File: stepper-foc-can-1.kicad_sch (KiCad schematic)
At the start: 31 parts, among them J1 TC2030, J2 Conn_01x02, U1 STM32G474RBTx, U2 MX25947, Y1 Crystal_GND24

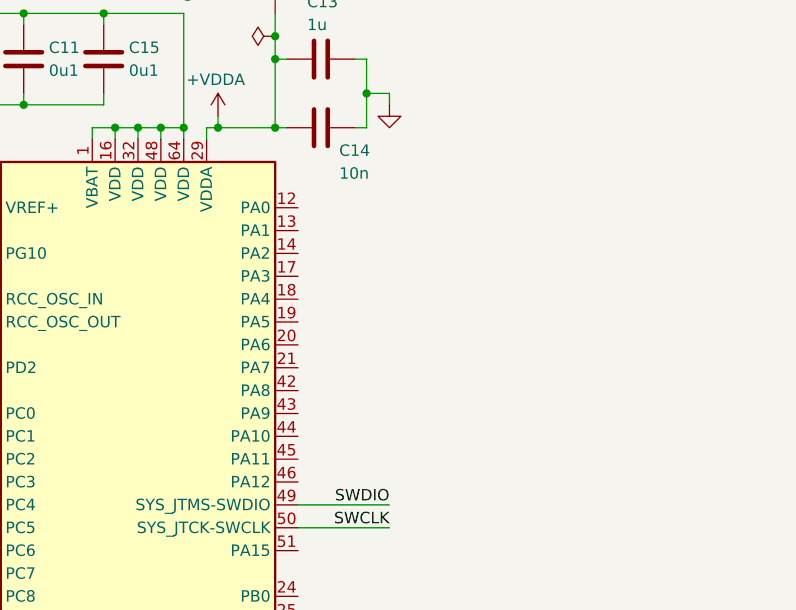
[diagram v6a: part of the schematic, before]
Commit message: schem: add uart connctor
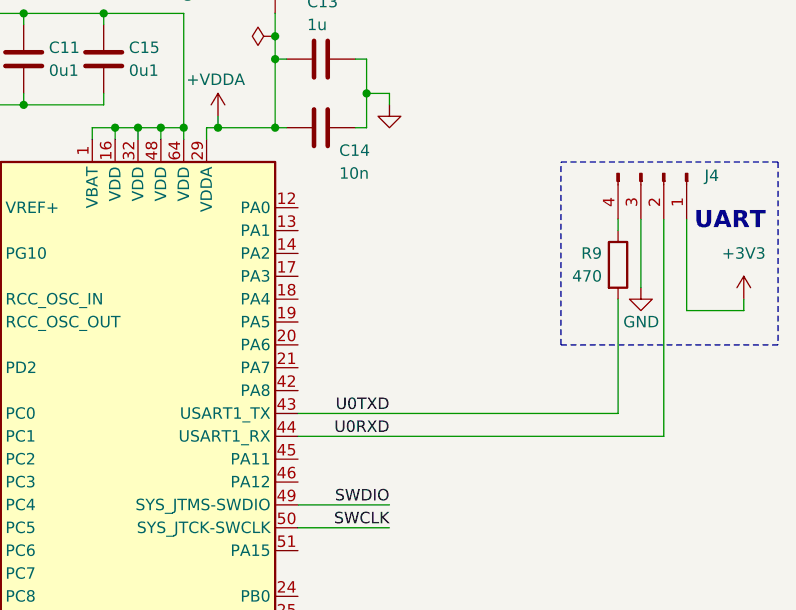
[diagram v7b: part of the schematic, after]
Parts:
- added J4: Conn_01x04_Pin, Connector_PinHeader_2.54mm:PinHeader_1x04_P2.54mm_Vertical, symbol Connector:Conn_01x04_Pin
- added R9: 470, Resistor_SMD:R_0402_1005Metric, symbol Device:R
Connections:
- net +3V3: now also J4.1 (Pin_1)
- net GND: now also J4.3 (Pin_3)
- net U0TXD: now reaches U1.43 (PA9)
- net U0TXD: now also R9.2
- net U0RXD: now reaches U1.44 (PA10)
- net U0RXD: now also J4.2 (Pin_2)
- new net: J4.4 (Pin_4), R9.1
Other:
- note added: "UART"

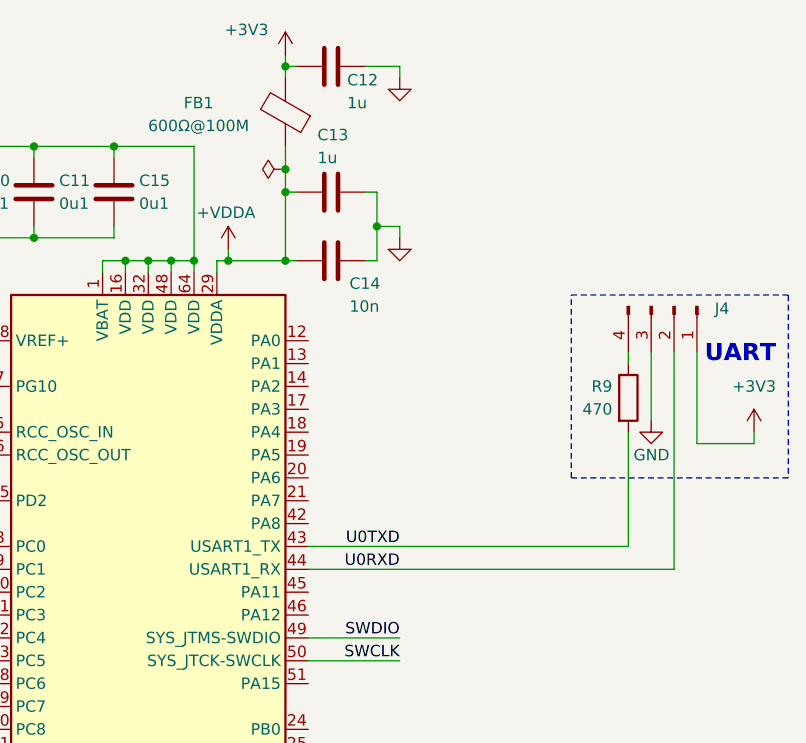
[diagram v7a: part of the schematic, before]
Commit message: schem: fix uart pins
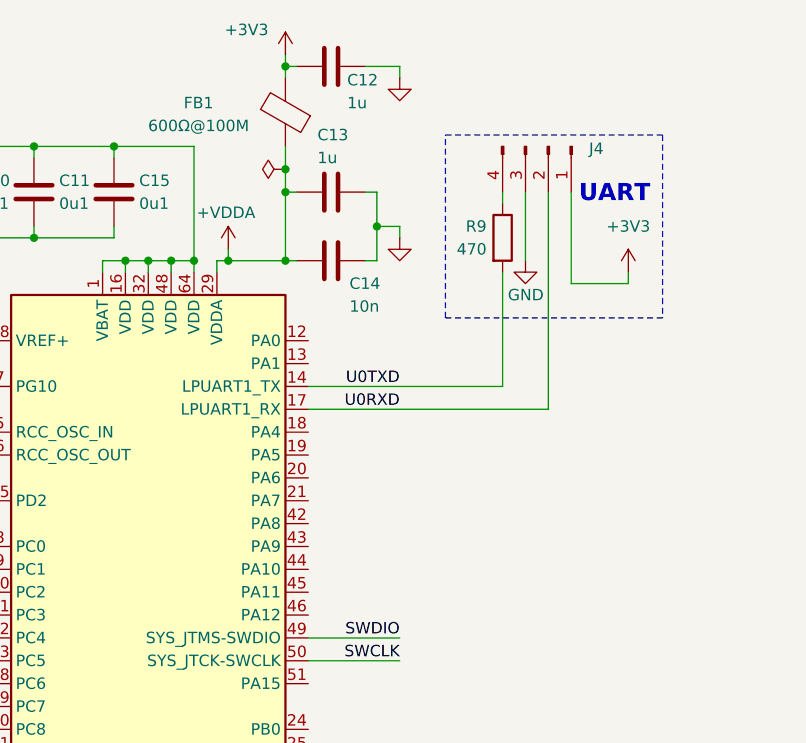
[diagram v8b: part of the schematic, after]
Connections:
- net U0RXD: now also U1.17 (PA3); no longer U1.44 (PA10)
- net U0TXD: now also U1.14 (PA2); no longer U1.43 (PA9)
